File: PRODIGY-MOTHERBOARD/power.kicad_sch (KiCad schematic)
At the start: 46 parts, among them J23 Barrel_Jack_MountingPin, U5 TPS22810DRV, U6 TPS54331DR, U7 TPS54331DR

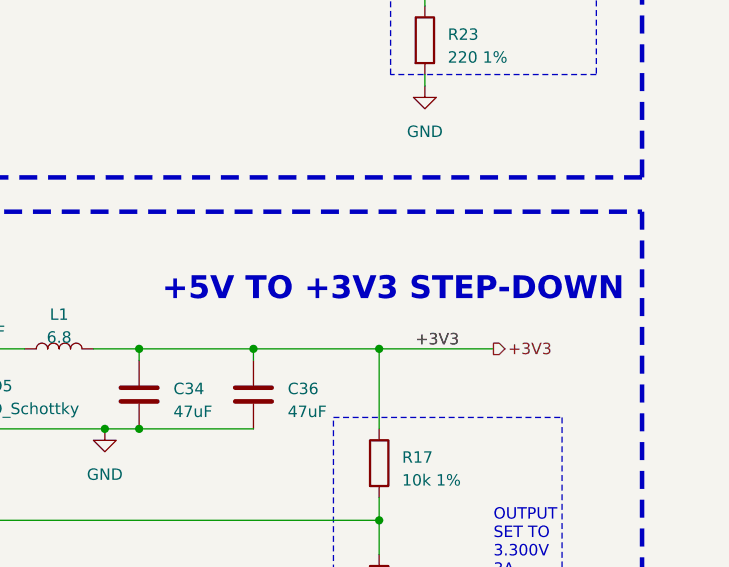
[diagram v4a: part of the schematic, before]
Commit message: Added pins to MCU. Added Decoder for SPI SS-Multiplexing.
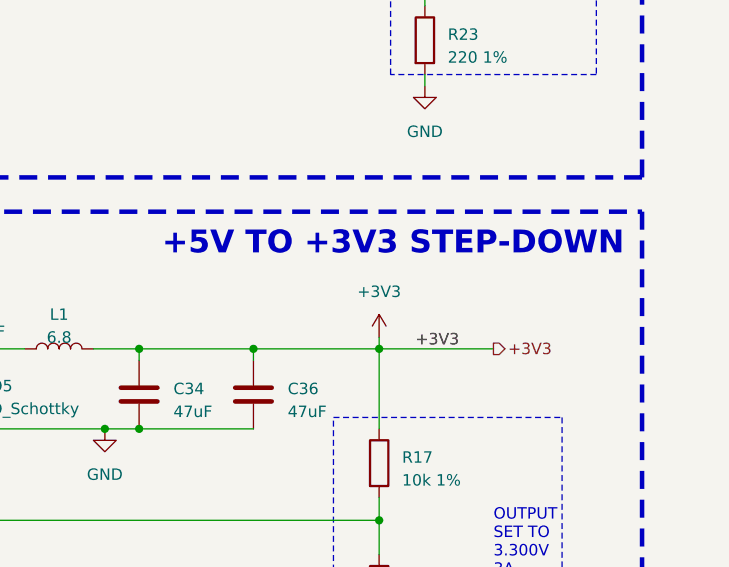
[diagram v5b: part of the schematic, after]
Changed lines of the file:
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@@
+	(wire
+		(pts
+			(xy 252.73 107.95) (xy 252.73 109.22)
+		)
+		(stroke
+			(width 0)
+			(type default)
+		)
+	)
 	(wire
 		(pts
@@
 	(text "+5V TO +3V3 STEP-DOWN"
 		(exclude_from_sim no)
-		(at 228.6 104.14 0)
+		(at 228.6 99.06 0)
 		(effects
 			(font
@@
 		)
 	)
+	(symbol
+		(lib_id "power:+3V3")
+		(at 252.73 107.95 0)
+		(unit 1)
+		(exclude_from_sim no)
+		(in_bom yes)
+		(on_board yes)
+		(dnp no)
+		(fields_autoplaced yes)
+		(property "Reference" "#PWR0202"
+			(at 252.73 111.76 0)
+			(effects
+				(font
+					(size 1.27 1.27)
+				)
+				(hide yes)
+			)
+		)
+		(property "Value" "+3V3"
+			(at 252.73 102.87 0)
+			(effects
+				(font
+					(size 1.27 1.27)
+				)
+			)
+		)
+		(property "Footprint" ""
+			(at 252.73 107.95 0)
+			(effects
+				(font
+					(size 1.27 1.27)
+				)
+				(hide yes)
+			)
+		)
+		(property "Datasheet" ""
+			(at 252.73 107.95 0)
+			(effects
+				(font
+					(size 1.27 1.27)
+				)
+				(hide yes)
+			)
+		)
+		(property "Description" "Power symbol creates a global label with name \"+3V3\""
+			(at 252.73 107.95 0)
+			(effects
+				(font
+					(size 1.27 1.27)
+				)
+				(hide yes)
+			)
+		)
+		(pin "1"
+		)
+		(instances
+			(project "PRODIGY-MOTHERBOARD"
+				(path "/f1c25860-8989-4190-bd24-2491d23ca7d9/7df83d4f-8c4f-4445-bdae-bd2c13239983"
+					(reference "#PWR0202")
+					(unit 1)
+				)
+			)
+		)
+	)

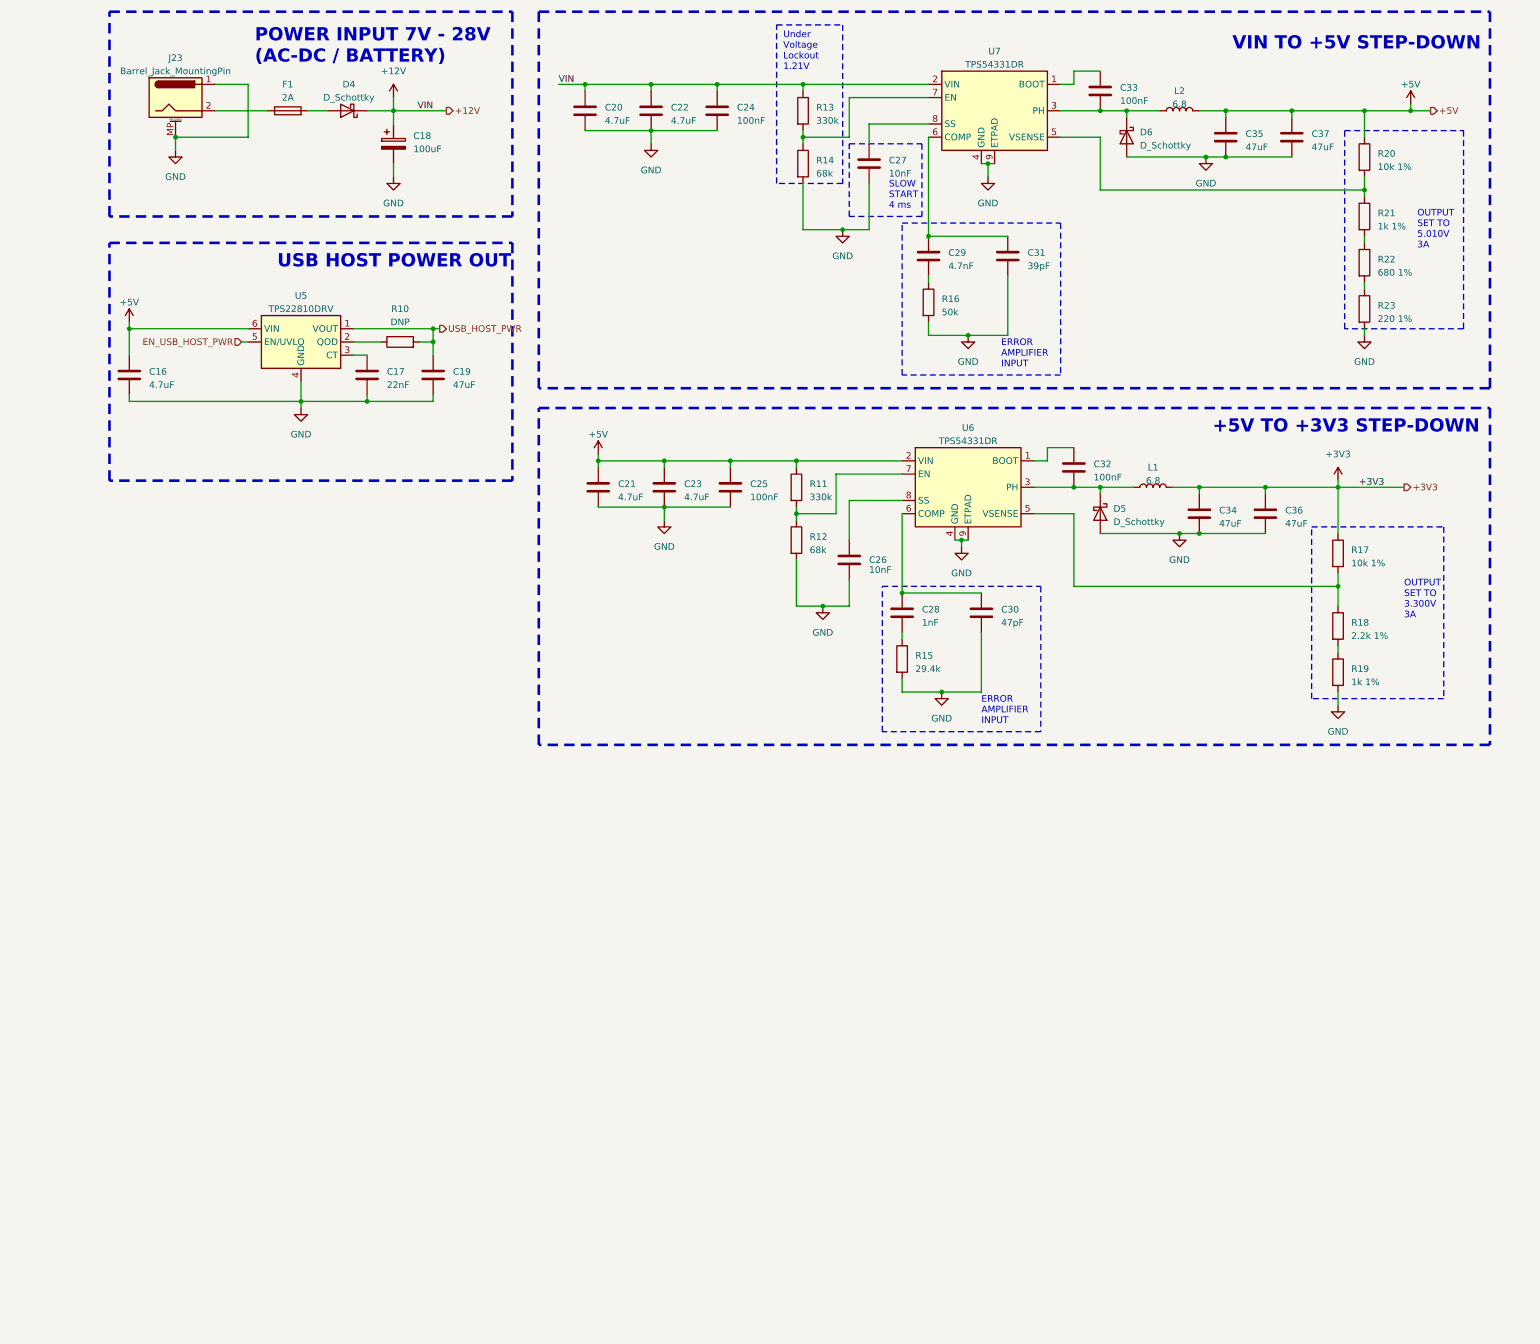
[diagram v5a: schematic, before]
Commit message: Added proper debounce filter elements to buttons.
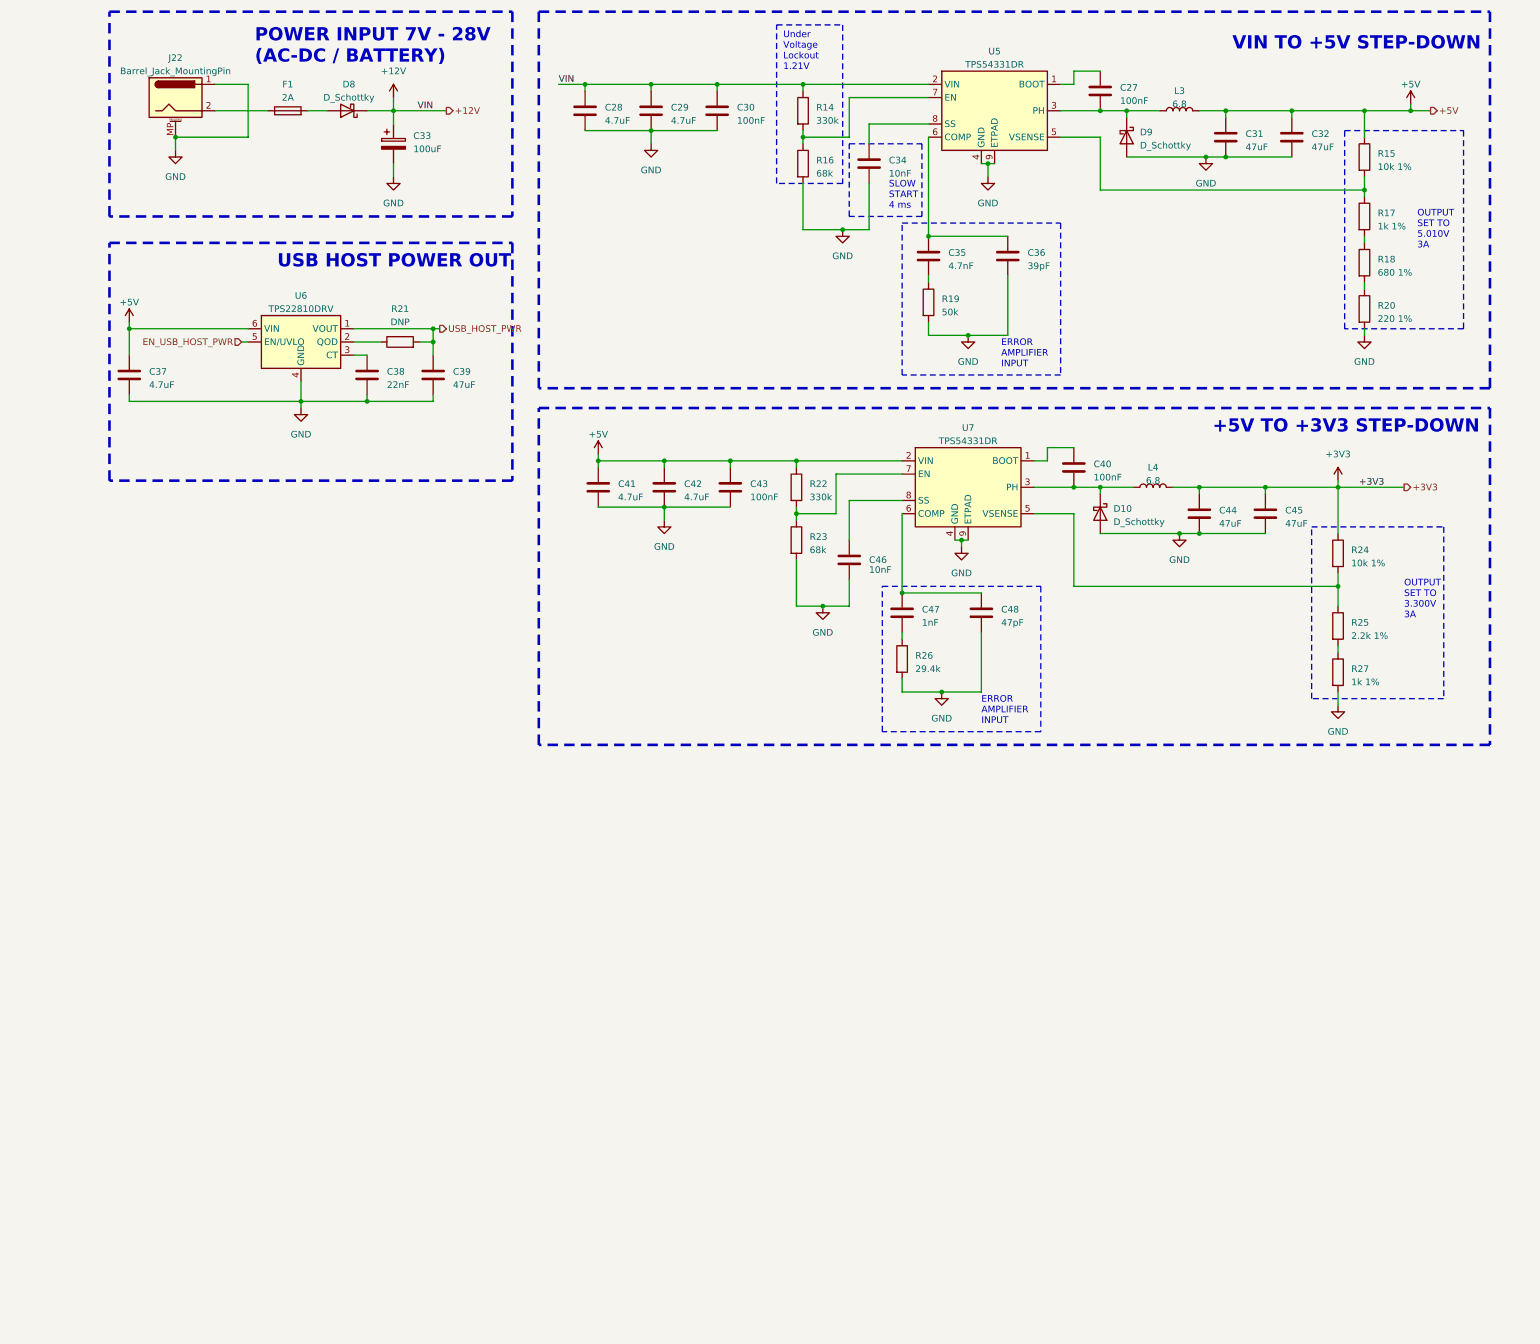
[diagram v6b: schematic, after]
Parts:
- renumbered C33 to C27, C20 to C28, C22 to C29, C24 to C30, C35 to C31, C37 to C32, C18 to C33, C27 to C34, C29 to C35, C31 to C36, C16 to C37, C17 to C38, C19 to C39, C32 to C40, C21 to C41, C23 to C42, C25 to C43, C34 to C44, C36 to C45, C26 to C46, C28 to C47, C30 to C48, D5 to D10, D4 to D8, D6 to D9, J23 to J22, L2 to L3, L1 to L4, R13 to R14, R20 to R15, R14 to R16, R21 to R17, R22 to R18, R16 to R19, R23 to R20, R10 to R21, R11 to R22, R12 to R23, R17 to R24, R18 to R25, R15 to R26, R19 to R27, U7 to U5, U5 to U6, U6 to U7

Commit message: Submitted V0 for evaluation. Avaiting feedback.
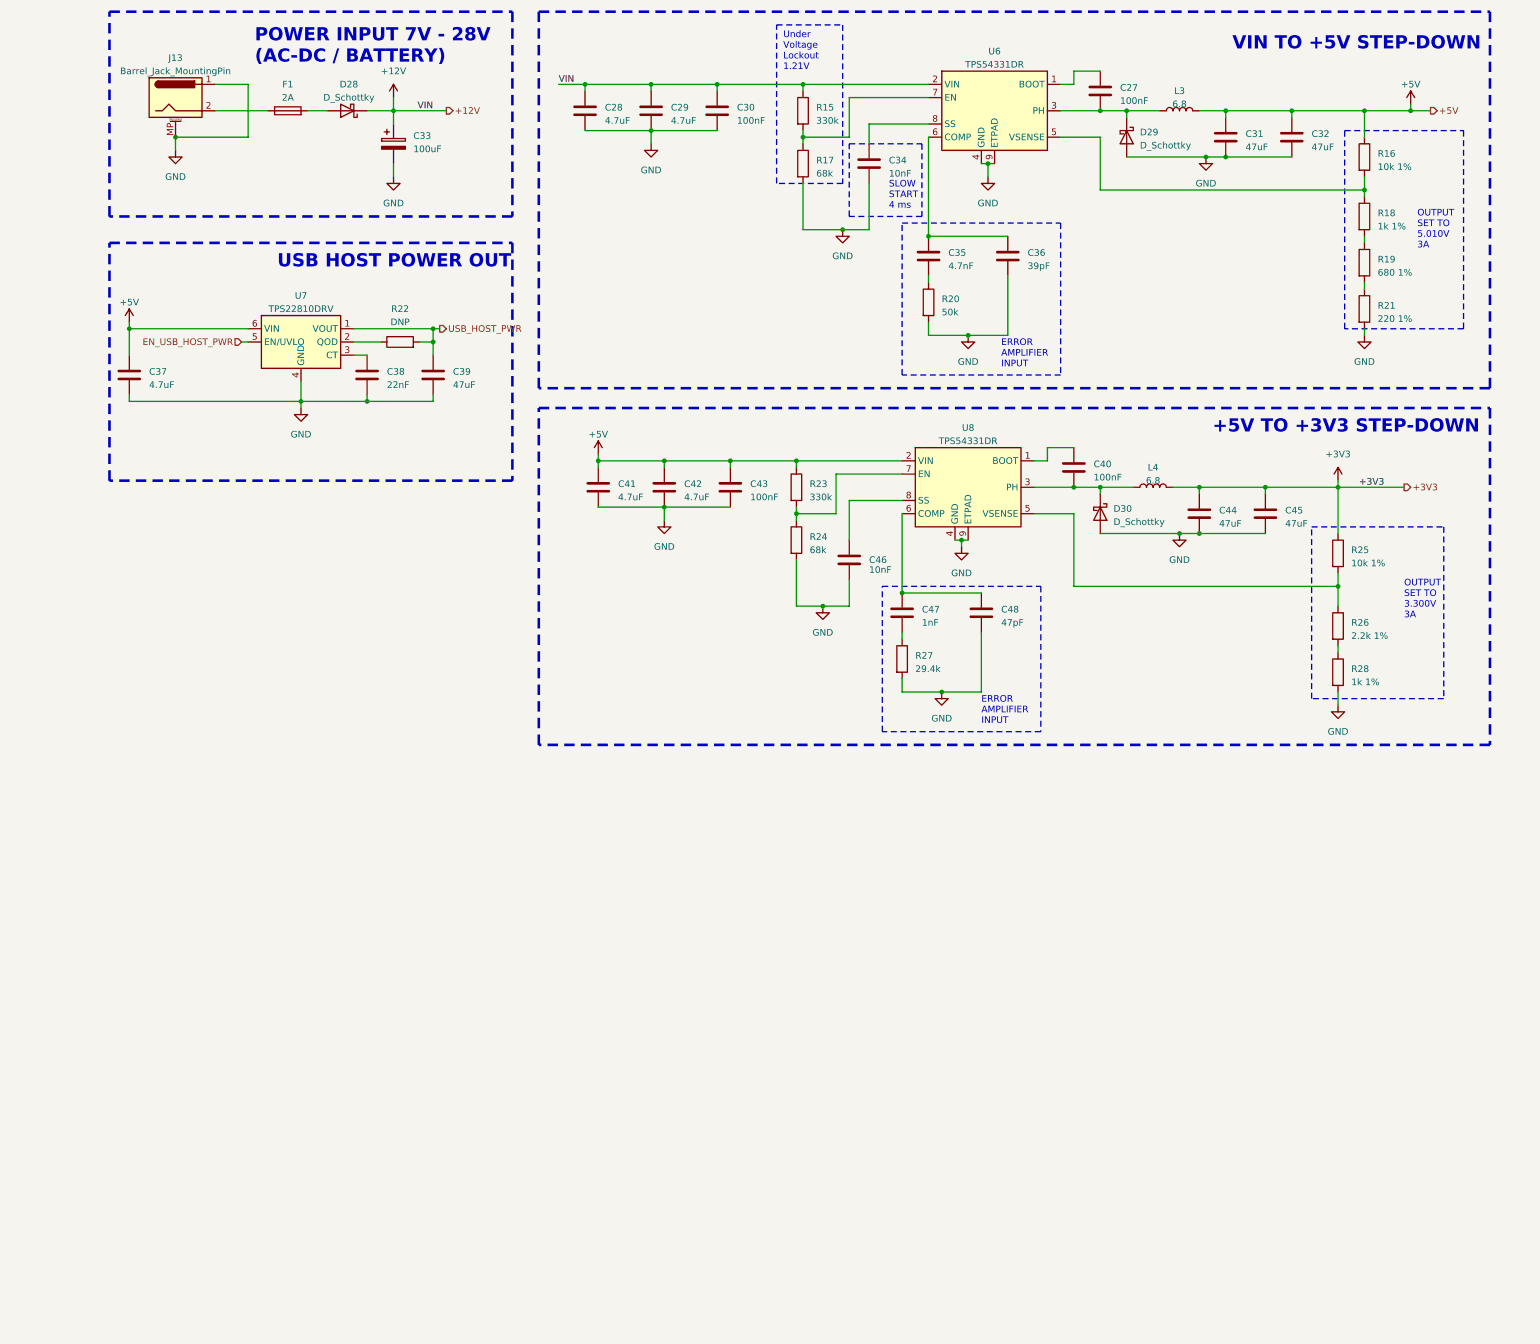
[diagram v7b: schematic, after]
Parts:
- renumbered D8 to D28, D9 to D29, D10 to D30, J22 to J13, R14 to R15, R15 to R16, R16 to R17, R17 to R18, R18 to R19, R19 to R20, R20 to R21, R21 to R22, R22 to R23, R23 to R24, R24 to R25, R25 to R26, R26 to R27, R27 to R28, U5 to U6, U6 to U7, U7 to U8

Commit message: Finished v0.1 schematic.
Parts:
- added C22, C23: 47uF, Capacitor_SMD:CP_Elec_6.3x5.8, symbol Device:C_Polarized
- added L1: 100uH, symbol Device:L_Ferrite
- renumbered C30 to C10, C43 to C11, C46 to C12, C34 to C13, C47 to C14, C35 to C15, C48 to C16, C36 to C17, C40 to C18, C27 to C19, C37 to C2, C44 to C20, C31 to C21, C45 to C24, C32 to C25, C38 to C3, C33 to C4, C39 to C5, C28 to C6, C41 to C7, C29 to C8, C42 to C9, D28 to D6, D30 to D7, D29 to D8, J13 to J5, L4 to L2, R27 to R10, R20 to R11, R25 to R12, R26 to R13, R28 to R14, R16 to R15, R18 to R16, R19 to R17, R21 to R18, R22 to R5, R23 to R6, R24 to R7, R15 to R8, R17 to R9, U7 to U1, U8 to U2, U6 to U3
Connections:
- net +3V3: now also C22.1, L1.1
- net +5V: now also C23.1
- net GND: now also C22.2, C23.2
- new net +3.3VA: L1.2
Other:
- note added: "Analog Power"
